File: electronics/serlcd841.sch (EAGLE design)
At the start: 12 parts, among them IC1 T841, J1 AVRISP, Q1 3904

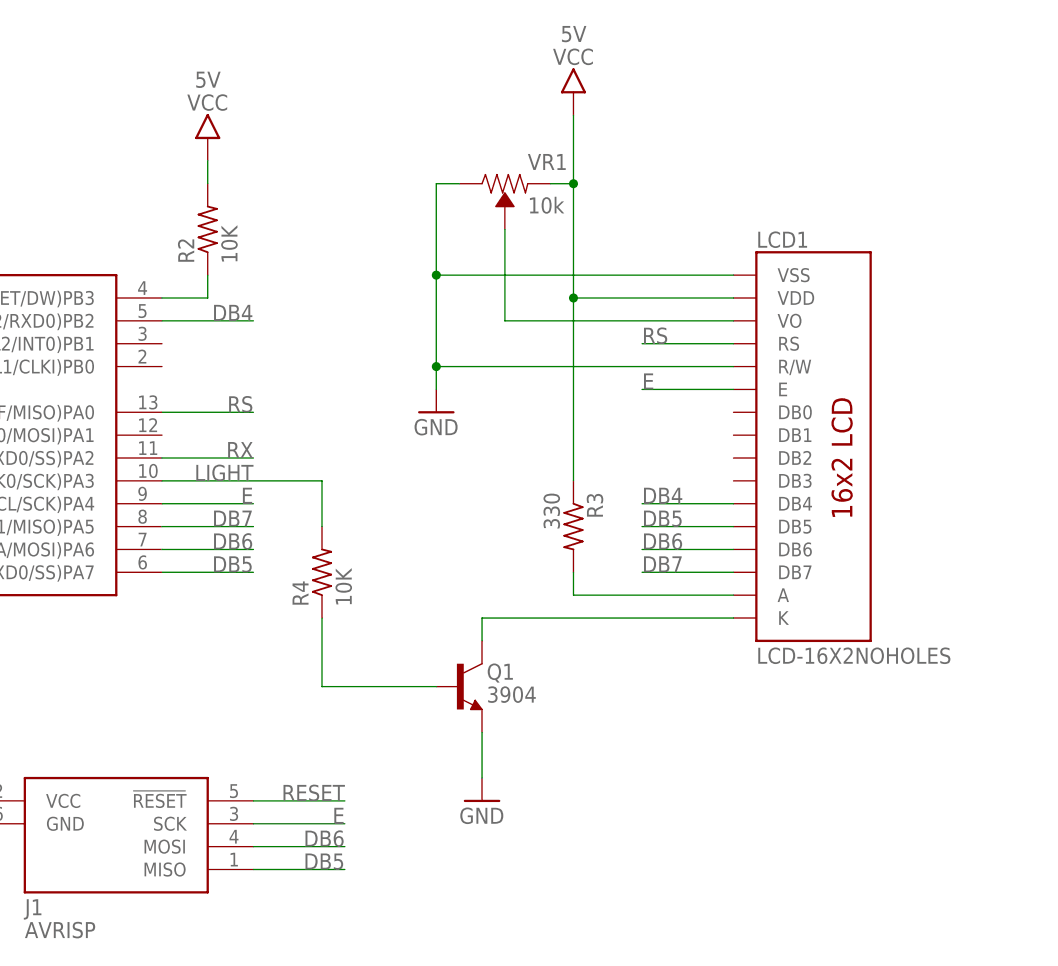
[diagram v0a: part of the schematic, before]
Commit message: updated footprint for lcd, layout tweaks, switched some pins.
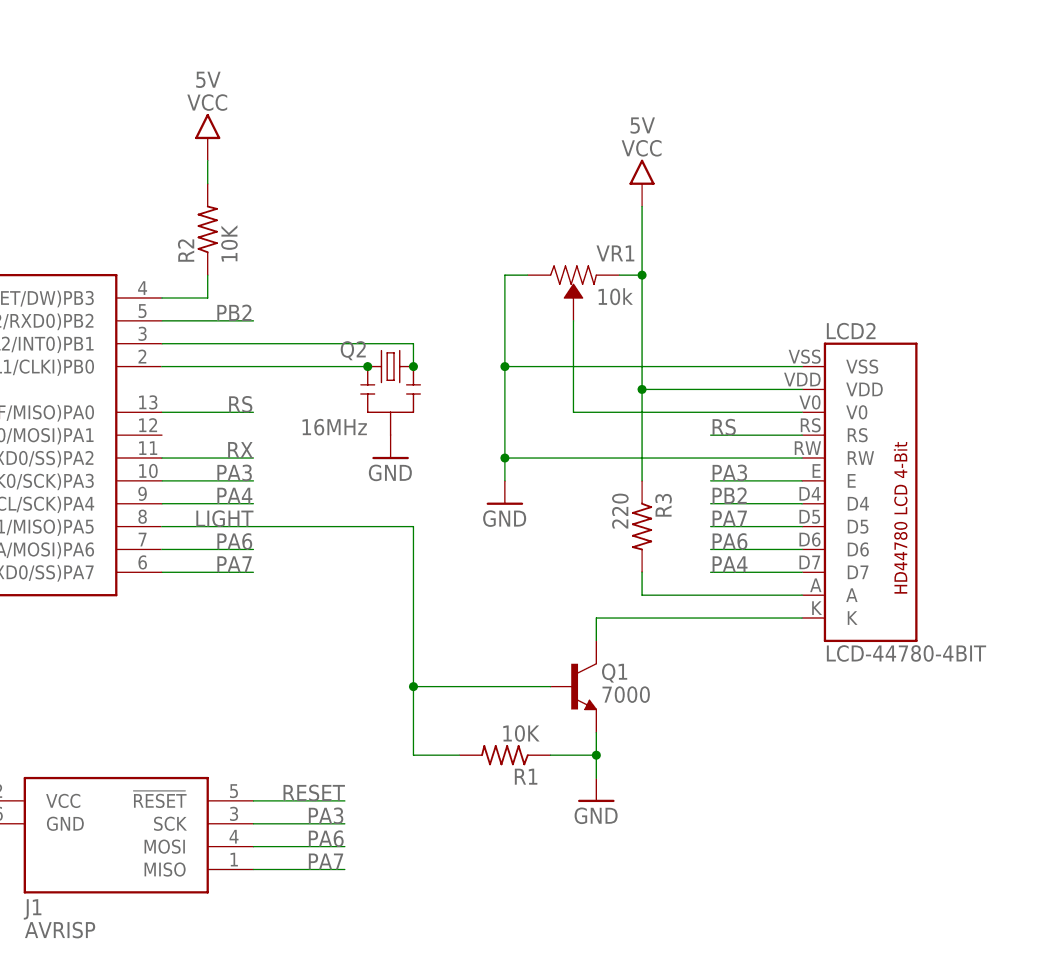
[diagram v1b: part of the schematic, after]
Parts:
- removed LCD1: LCD-16X2NOHOLES, SparkFun-Displays:LCD-16X2NOHOLES
- removed R4: 10K, bt_rcl:R0603
- added LCD2: LCD-44780-4BIT, bt_display:LCD-44780-4BIT
- added Q2: 16MHz, bt_crystal:RESONATOR_CSTCE_V_C
- added R1: 10K, bt_rcl:R0603
- Q1: value 3904 -> 7000
- R3: value 330 -> 220
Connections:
- removed net DB4: IC1.(PCINT10/ADC8/CLKO/TOCC7/ICP2/RXD0)PB2, LCD1.DB4
- removed net DB5: IC1.(PCINT7/ADC7/TOCC6/ICP1/TXD0/SS)PA7, J1.MISO, LCD1.DB5
- removed net DB6: IC1.(PCINT6/ADC6/ACO1/TOCC5/XCK1/SDA/MOSI)PA6, J1.MOSI, LCD1.DB6
- removed net DB7: IC1.(PCINT5/ADC5/ACO0/TOCC4/T2/TXD1/MISO)PA5, LCD1.DB7
- removed net E: IC1.(PCINT4/ADC4/AIN11/TOCC3/T1/RXD1/SCL/SCK)PA4, J1.SCK, LCD1.E
- removed net N$1: Q1.B, R4.1
- new net N$2: IC1.(PCINT8/ADC11/XTAL1/CLKI)PB0, Q2.X2
- new net N$3: IC1.(PCINT9/ADC10/XTAL2/INT0)PB1, Q2.X1
- new net PA3: IC1.(PCINT3/ADC3/AIN10/TOCC2/T0/XCK0/SCK)PA3, J1.SCK, LCD2.E
- new net PA4: IC1.(PCINT4/ADC4/AIN11/TOCC3/T1/RXD1/SCL/SCK)PA4, LCD2.D7
- new net PA6: IC1.(PCINT6/ADC6/ACO1/TOCC5/XCK1/SDA/MOSI)PA6, J1.MOSI, LCD2.D6
- new net PA7: IC1.(PCINT7/ADC7/TOCC6/ICP1/TXD0/SS)PA7, J1.MISO, LCD2.D5
- new net PB2: IC1.(PCINT10/ADC8/CLKO/TOCC7/ICP2/RXD0)PB2, LCD2.D4
- net A: now also LCD2.A; no longer LCD1.A
- net GND: now also LCD2.RW, LCD2.VSS, Q2.GND, R1.1; no longer LCD1.R/W, LCD1.VSS
- net K: now also LCD2.K; no longer LCD1.K
- net LIGHT: now also IC1.(PCINT5/ADC5/ACO0/TOCC4/T2/TXD1/MISO)PA5, Q1.B, R1.2; no longer IC1.(PCINT3/ADC3/AIN10/TOCC2/T0/XCK0/SCK)PA3, R4.2
- net RS: now also LCD2.RS; no longer LCD1.RS
- net VCC: now also LCD2.VDD; no longer LCD1.VDD
- net VO: now also LCD2.V0; no longer LCD1.VO
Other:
- moved on the sheet: Q1, R3, VR1

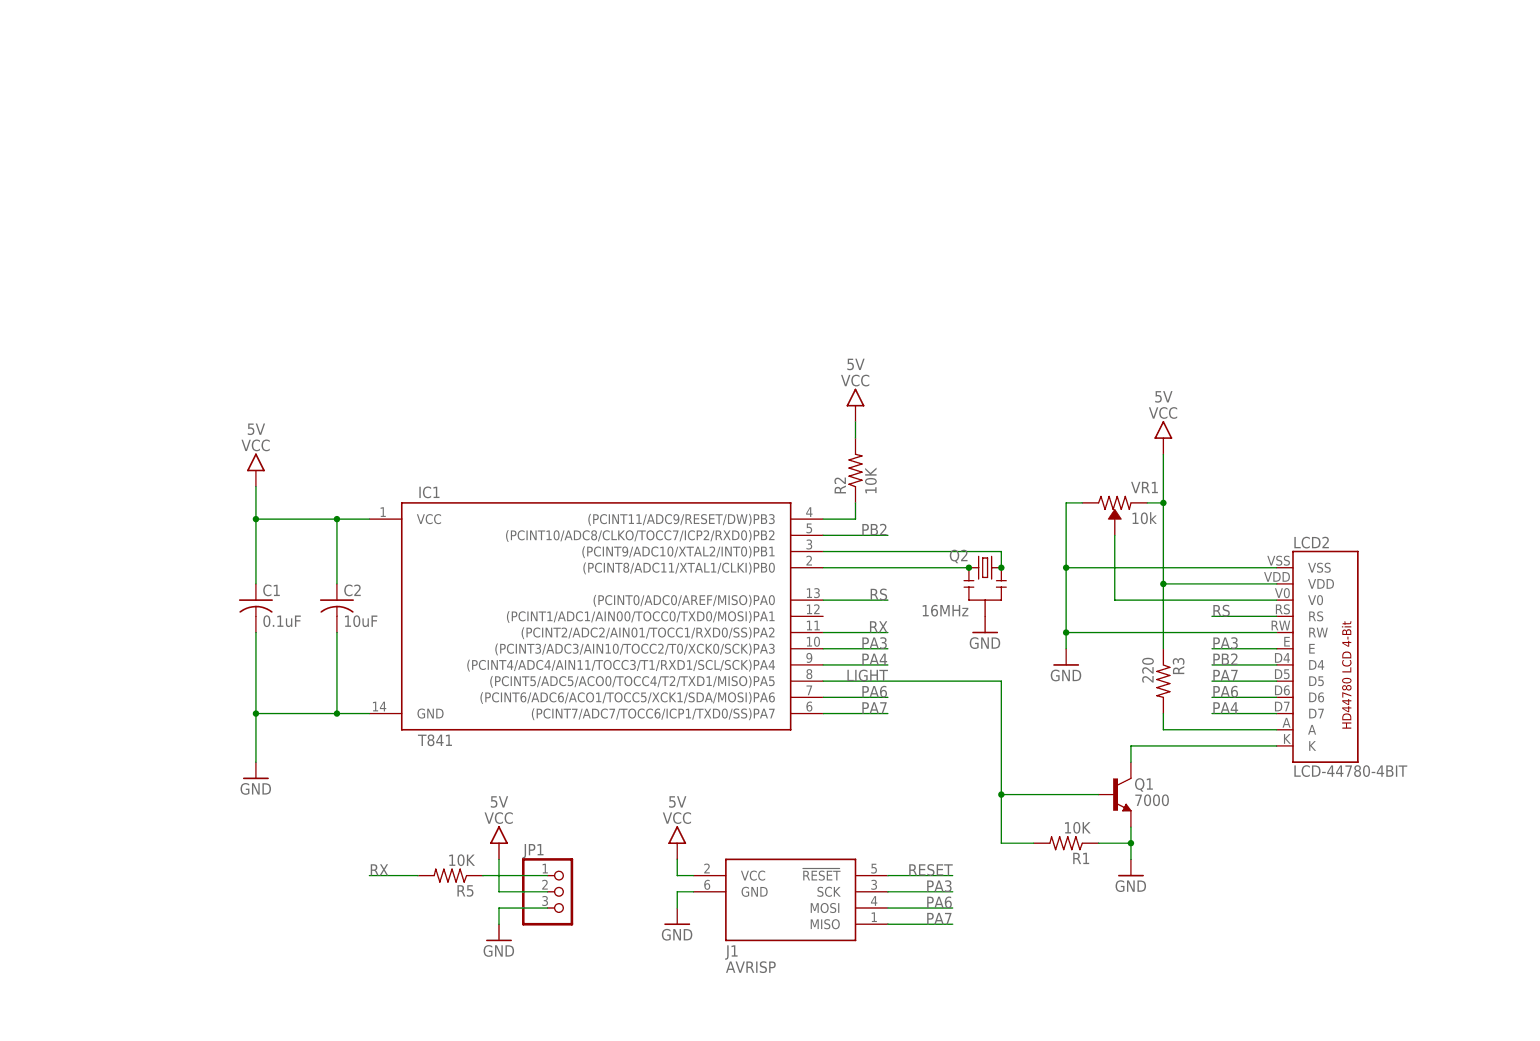
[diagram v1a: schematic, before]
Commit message: Corrected ISP connections, removed transistor for
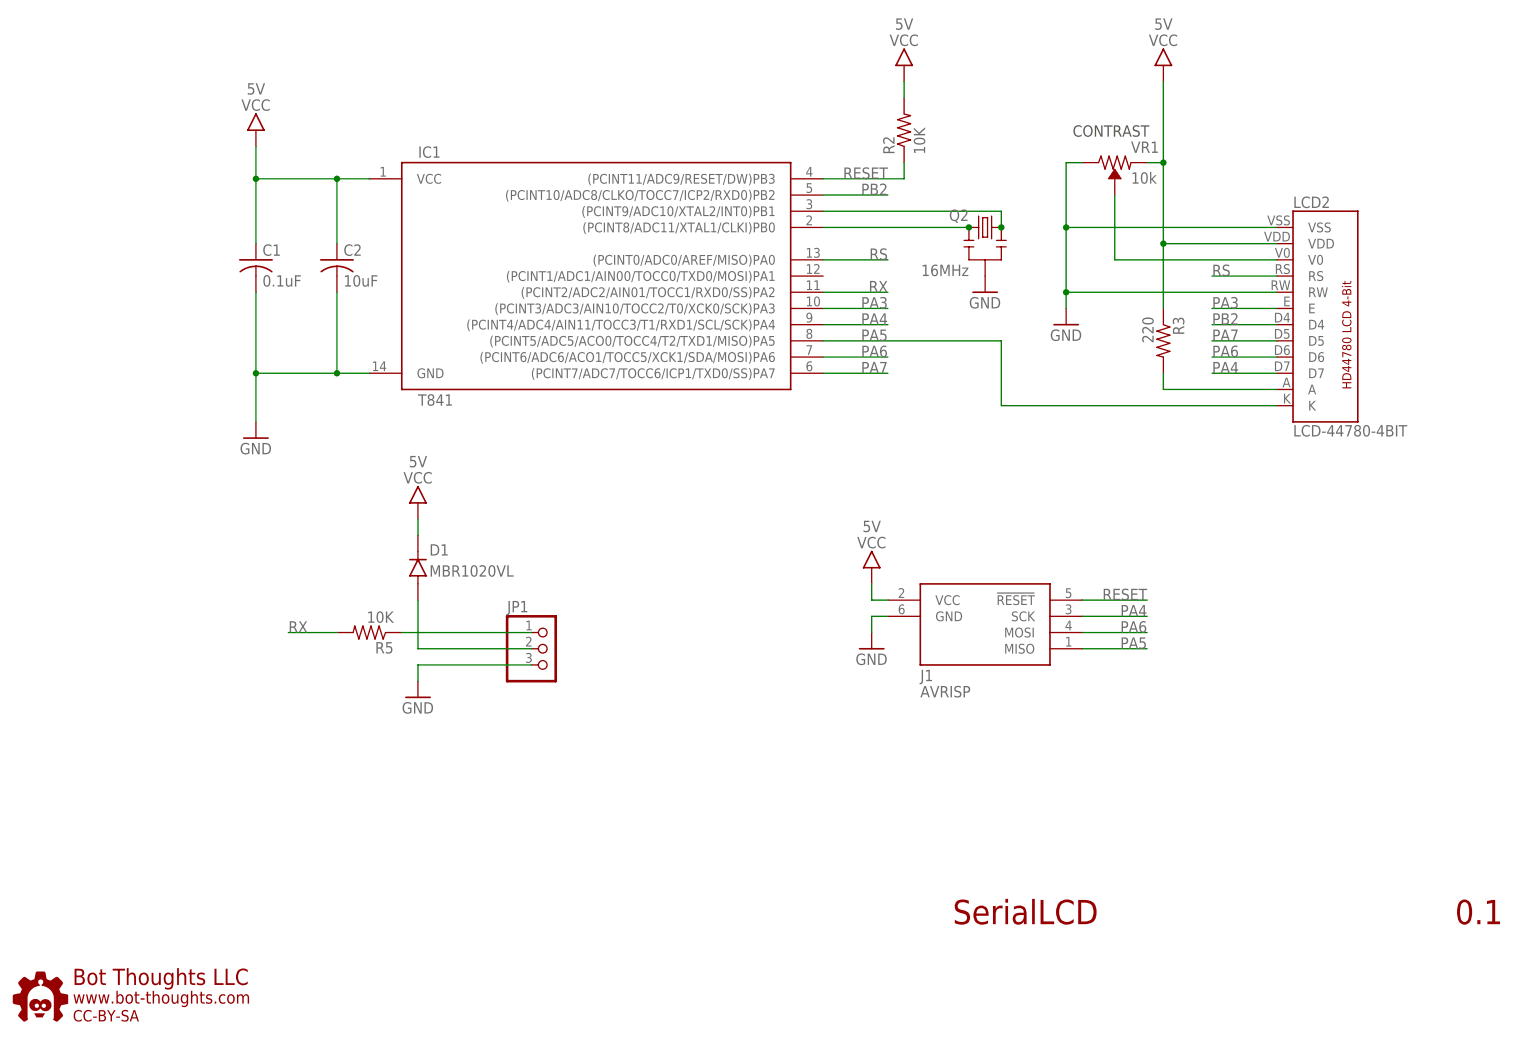
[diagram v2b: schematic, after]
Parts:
- removed Q1: 7000, bt_transistor:BJT-NPNSOT23
- removed R1: 10K, bt_rcl:R0603
- added D1: MBR1020VL, bt_diode:DIODE_SOD123FL
- added U$6: BTLOGO-LOGO-MD, bt:BTLOGO-LOGO-MD
- J1: device bt_avr:AVRISP6_COMPACT -> bt_avr:AVRISP6_TP
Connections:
- removed net K: LCD2.K, Q1.C
- removed net LIGHT: IC1.(PCINT5/ADC5/ACO0/TOCC4/T2/TXD1/MISO)PA5, Q1.B, R1.2
- new net N$1: D1.A, JP1.2
- new net PA5: IC1.(PCINT5/ADC5/ACO0/TOCC4/T2/TXD1/MISO)PA5, J1.MISO, LCD2.K
- net GND: no longer Q1.E, R1.1
- net PA3: no longer J1.SCK
- net PA4: now also J1.SCK
- net PA7: no longer J1.MISO
- net VCC: now also D1.C; no longer JP1.2
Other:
- note added: "0.1"
- note added: "CONTRAST"
- note added: "SerialLCD"
- moved on the sheet: C1, C2, IC1, J1, JP1, LCD2, Q2, R2, R3, R5, VR1

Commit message: i don't remember :(
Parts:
- added Q1: 2n3904, bt_transistor:BJT-NPNSOT23
- added R1: 10K, bt_rcl:R0603
- J1: device bt_avr:AVRISP6_TP -> bt_avr:AVRISP6_COMPACT
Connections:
- new net N$4: Q1.B, R1.2
- new net N$5: LCD2.K, Q1.C
- net GND: now also Q1.E
- net PA5: now also R1.1; no longer LCD2.K
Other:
- note added: "0.2"
- note removed: "0.1"
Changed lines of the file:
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@@
 <part name="GND4" library="bt" deviceset="GND" device=""/>
 <part name="R5" library="bt_rcl" deviceset="R" device="0603" value="10K"/>
-<part name="J1" library="bt_avr" deviceset="AVRISP6" device="_TP" value="AVRISP"/>
+<part name="J1" library="bt_avr" deviceset="AVRISP6" device="_COMPACT" value="AVRISP"/>
 <part name="U$5" library="bt" deviceset="VCC" device="" value="5V"/>
 <part name="GND5" library="bt" deviceset="GND" device=""/>
@@
 <part name="FRAME1" library="bt" deviceset="LETTER_L" device=""/>
 <part name="D1" library="bt_diode" deviceset="DIODE" device="_SOD123FL" value="MBR1020VL"/>
+<part name="Q1" library="bt_transistor" deviceset="BJT-NPN" device="SOT23" value="2n3904"/>
+<part name="GND1" library="bt" deviceset="GND" device=""/>
+<part name="R1" library="bt_rcl" deviceset="R" device="0603" value="10K"/>
 </parts>
 <sheets>
@@
 <plain>
 <text x="149.86" y="17.78" size="3.81" layer="94">SerialLCD</text>
-<text x="228.6" y="17.78" size="3.81" layer="94">0.1</text>
+<text x="228.6" y="17.78" size="3.81" layer="94">0.2</text>
 <text x="168.656" y="141.224" size="1.778" layer="97">CONTRAST</text>
 </plain>
@@
 <attribute name="VALUE" x="67.818" y="72.263" size="1.778" layer="96"/>
 </instance>
+<instance part="Q1" gate="Q2" x="190.5" y="91.44"/>
+<instance part="GND1" gate="1" x="193.04" y="83.82"/>
+<instance part="R1" gate="R1" x="170.18" y="91.44"/>
 </instances>
 <busses>
@@
 <pinref part="GND6" gate="1" pin="GND"/>
 </segment>
+<segment>
+<pinref part="Q1" gate="Q2" pin="E"/>
+<pinref part="GND1" gate="1" pin="GND"/>
+</segment>
 </net>
 <net name="RESET" class="0">
@@
 <net name="PA5" class="0">
 <segment>
-<wire x1="200.66" y1="99.06" x2="157.48" y2="99.06" width="0.1524" layer="91"/>
-<pinref part="LCD2" gate="LCD1" pin="K"/>
 <pinref part="IC1" gate="IC1" pin="(PCINT5/ADC5/ACO0/TOCC4/T2/TXD1/MISO)PA5"/>
 <label x="139.7" y="109.22" size="1.778" layer="95" rot="MR0"/>
-<wire x1="157.48" y1="109.22" x2="157.48" y2="99.06" width="0.1524" layer="91"/>
+<wire x1="157.48" y1="109.22" x2="157.48" y2="91.44" width="0.1524" layer="91"/>
 <wire x1="129.54" y1="109.22" x2="157.48" y2="109.22" width="0.1524" layer="91"/>
+<pinref part="R1" gate="R1" pin="1"/>
+<wire x1="165.1" y1="91.44" x2="157.48" y2="91.44" width="0.1524" layer="91"/>
 </segment>
 <segment>
@@
 </segment>
 </net>
+<net name="N$4" class="0">
+<segment>
+<pinref part="Q1" gate="Q2" pin="B"/>
+<pinref part="R1" gate="R1" pin="2"/>
+<wire x1="175.26" y1="91.44" x2="187.96" y2="91.44" width="0.1524" layer="91"/>
+</segment>
+</net>
+<net name="N$5" class="0">
+<segment>
+<pinref part="LCD2" gate="LCD1" pin="K"/>
+<wire x1="200.66" y1="99.06" x2="193.04" y2="99.06" width="0.1524" layer="91"/>
+<pinref part="Q1" gate="Q2" pin="C"/>
+<wire x1="193.04" y1="96.52" x2="193.04" y2="99.06" width="0.1524" layer="91"/>
+</segment>
+</net>
